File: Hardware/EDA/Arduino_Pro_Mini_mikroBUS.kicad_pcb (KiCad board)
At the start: 4 copper layers, 38.1 x 69.8 mm, 36 parts, among them CON1 BARREL_JACK, J1 HEADER_F_2.54MM_1R8P_ST_AU_PTH, J2 HEADER_F_2.54MM_1R8P_ST_AU_PTH, J3 HEADER_F_2.54MM_1R12P_ST_AU_P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, J4 HEADER_F_2.54MM_1R12P_ST_AU_P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, J5 Molex_0475710001, J6 HEADER_F_2.54MM_1R2P_ST_AU_PTH, M1 FID, M2 FID, M3 FID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

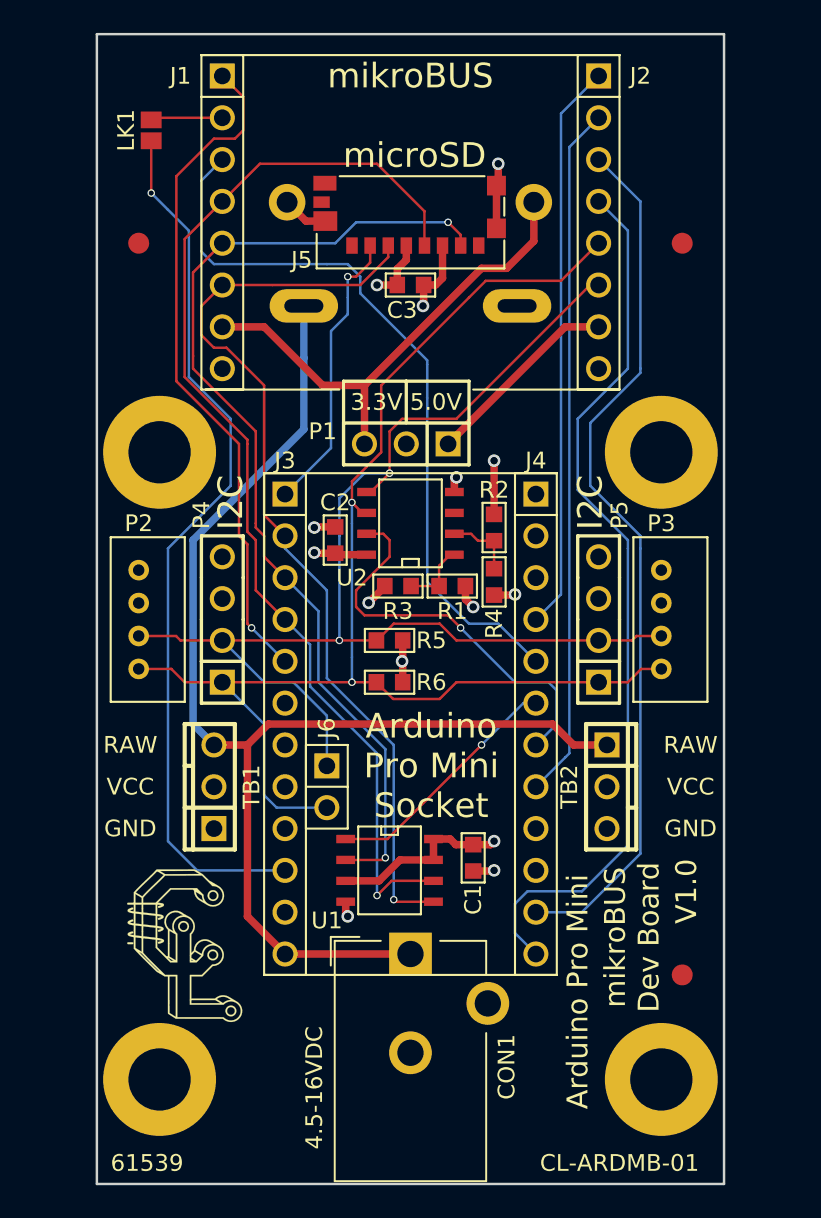
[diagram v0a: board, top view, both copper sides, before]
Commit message: Removed barrel jack connector due to interference with Arduino Pro Mini. Updated schematic, layout and generated new gerbers. Added BOM file.
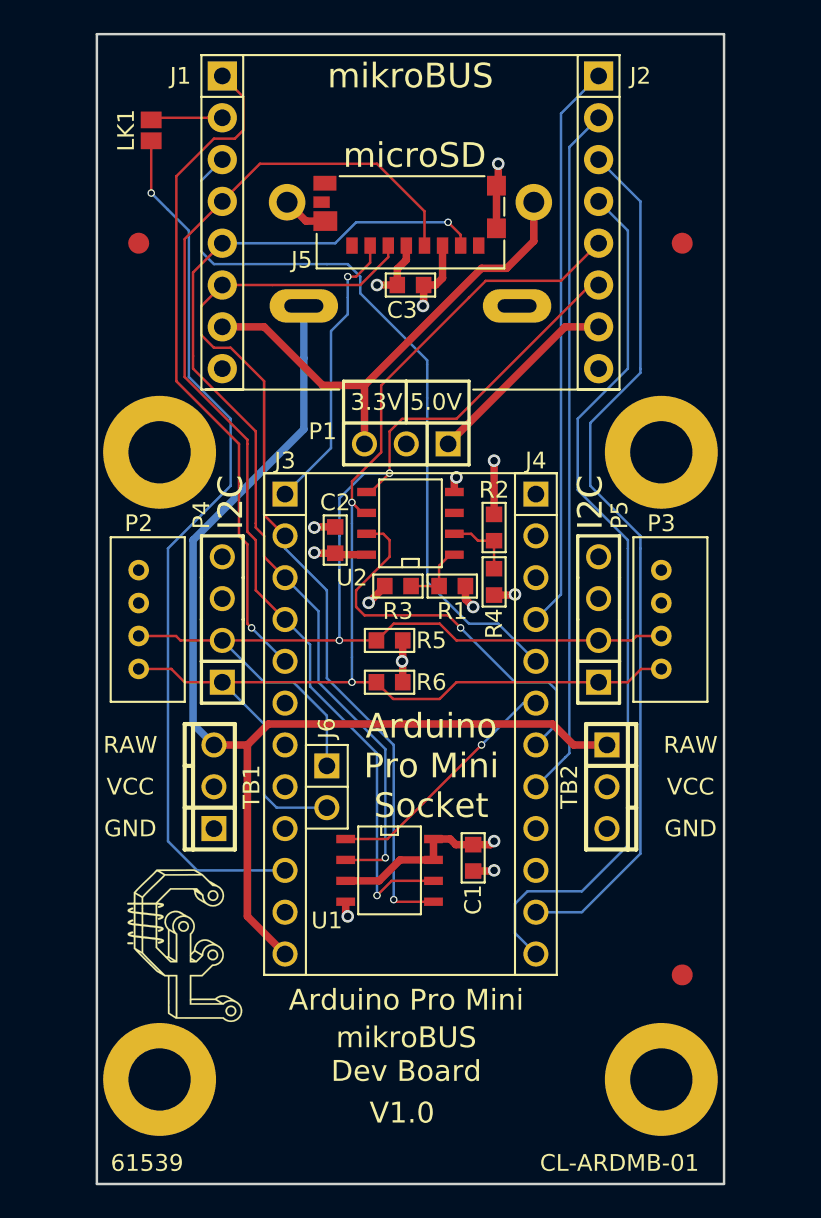
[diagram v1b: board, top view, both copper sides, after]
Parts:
- removed CON1: BARREL_JACK, Connect:Barrel_Jack_CUI_PJ-102AH
- TB2: footprint Terminal_Block:TB_100MIL_1R3P_PTH -> TB_100MIL_1R3P_PTH
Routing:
- net RAW: track 76.2 -> 68.6 mm
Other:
- board text removed: "4.5-16VDC"

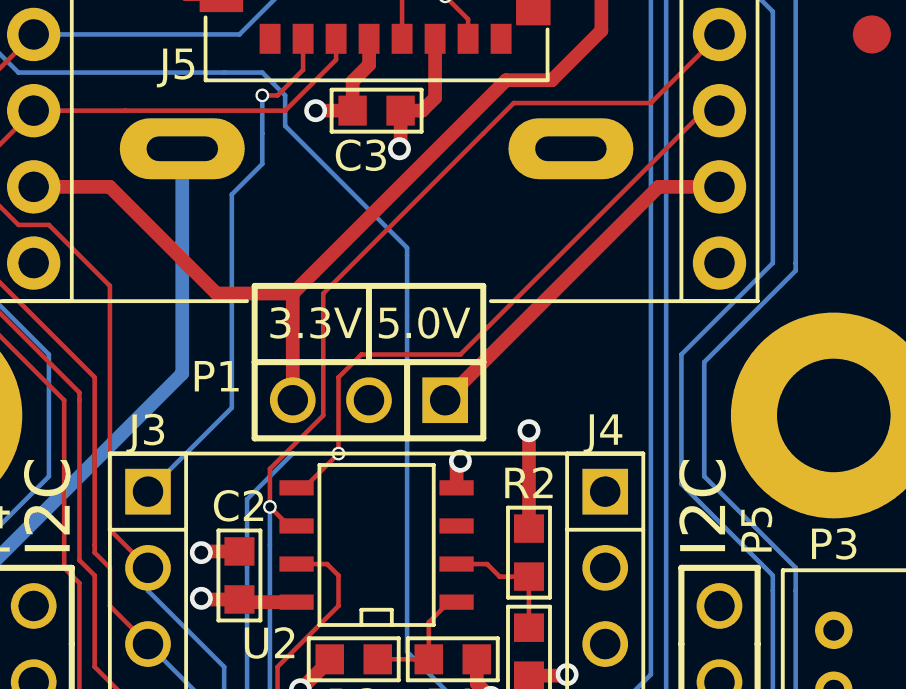
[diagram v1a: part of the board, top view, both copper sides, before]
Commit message: Move location of P1 down slightly to allow more room for mikroBUS module PCB.
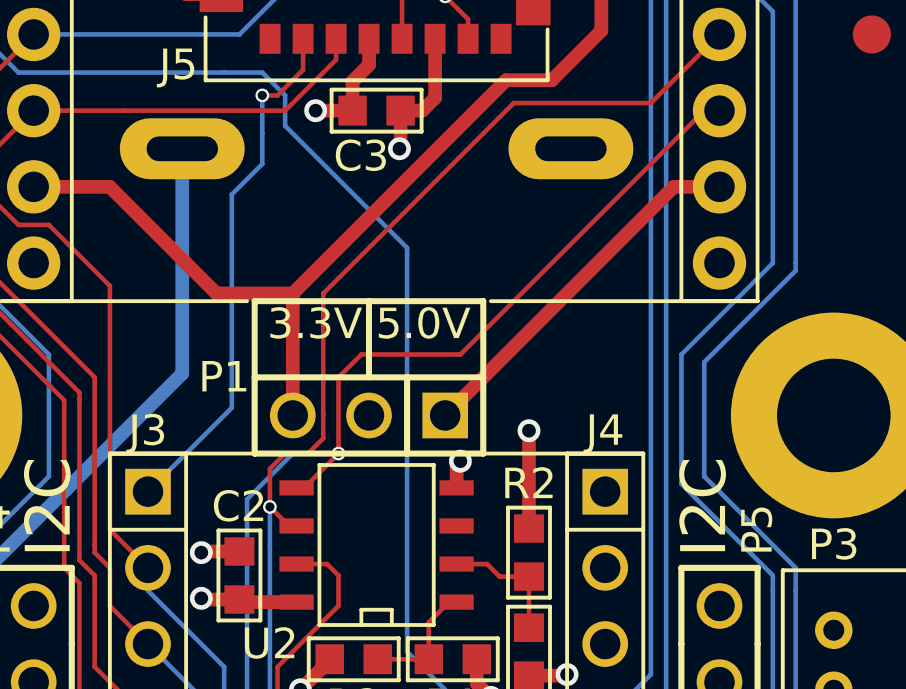
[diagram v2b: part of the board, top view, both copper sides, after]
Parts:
- moved P1 0.51 mm to (79.8, 57.1)
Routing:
- net 3.3V: track 29.9 -> 30.5 mm
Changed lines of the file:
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@@
     (thickness 1.6)
     (drawings 36)
-    (tracks 318)
+    (tracks 320)
     (zones 0)
     (modules 35)
@@
     (pad 2 thru_hole circle (at 27.8892 -7.493 90) (size 2.2225 2.2225) (drill 1.27) (layers *.Cu *.Mask)
       (net 2 GND))
-    (model C:/Engineering/KiCAD_Libraries/3D/Battery_Holders/VRML/KEYSTONE_2462.wrl
+    (model C:/Engineering/KiCAD_Libraries/3D/Battery_Holders/VRML/KEYSTONE_2462.wrl_
       (at (xyz 0.03 0 0))
       (scale (xyz 1 1 1))
@@
   )
   (module Header:HEADER_M_2.54MM_1R3P_ST_AU_PTH locked (layer F.Cu)
-    (at 79.756 56.642 180)
+    (at 79.756 57.15 180)
     (tags Header)
-    (fp_text reference P1 (at 5.08 0.762 180) (layer F.SilkS)
+    (fp_text reference P1 (at 4.826 1.27 180) (layer F.SilkS)
       (effects (font (size 1.016 1.016) (thickness 0.127)))
     )
@@
     (pad 1 thru_hole rect (at -2.54 0 180) (size 1.524 1.524) (drill 1.016) (layers *.Cu *.Mask)
       (net 11 5.0V))
-    (model C:\Engineering\KiCAD_Libraries\3D\Headers\HEADER_M_2.54MM_1R3P_ST_AU_PTH.wrl
+    (model C:/Engineering/KiCAD_Libraries/3D/Headers/VRML/HEADER_M_2.54MM_1R3P_ST_AU_PTH.wrl
       (at (xyz 0 0 0))
       (scale (xyz 1 1 1))
@@
     (pad 1 thru_hole rect (at -1.27 0 270) (size 1.524 1.524) (drill 1.016) (layers *.Cu *.Mask)
       (net 10 SDA))
-    (model C:/Engineering/KiCAD_Libraries/3D/Headers/VRML/HEADER_F_2.54MM_1R2P_ST_SN_PTH.wrl
+    (model C:/Engineering/KiCAD_Libraries/3D/Headers/VRML/HEADER_F_2.54MM_1R2P_ST_AU_PTH.wrl
       (at (xyz 0 0 0))
       (scale (xyz 1 1 1))
@@
   (gr_line (start 83.82 53.34) (end 92.71 53.34) (angle 90) (layer F.SilkS) (width 0.127))
   (gr_line (start 67.564 53.34) (end 75.692 53.34) (angle 90) (layer F.SilkS) (width 0.127))
-  (gr_line (start 75.946 52.832) (end 75.946 55.372) (angle 90) (layer F.SilkS) (width 0.2))
-  (gr_line (start 83.566 52.832) (end 83.566 55.372) (angle 90) (layer F.SilkS) (width 0.2))
-  (gr_line (start 79.756 52.832) (end 75.946 52.832) (angle 90) (layer F.SilkS) (width 0.2))
-  (gr_line (start 79.756 52.832) (end 83.566 52.832) (angle 90) (layer F.SilkS) (width 0.2))
-  (gr_line (start 79.756 55.372) (end 79.756 52.832) (angle 90) (layer F.SilkS) (width 0.2))
+  (gr_line (start 75.946 53.34) (end 75.946 55.88) (angle 90) (layer F.SilkS) (width 0.2))
+  (gr_line (start 83.566 53.34) (end 83.566 55.88) (angle 90) (layer F.SilkS) (width 0.2))
+  (gr_line (start 79.756 53.34) (end 75.946 53.34) (angle 90) (layer F.SilkS) (width 0.2))
+  (gr_line (start 79.756 53.34) (end 83.566 53.34) (angle 90) (layer F.SilkS) (width 0.2))
+  (gr_line (start 79.756 55.88) (end 79.756 53.34) (angle 90) (layer F.SilkS) (width 0.2))
   (gr_text RAW (at 97.028 74.93) (layer F.SilkS)
     (effects (font (size 1.016 1.016) (thickness 0.2032)))
@@
   (segment (start 78.66 45.292) (end 78.66 44.595) (width 0.1524) (layer F.Cu) (net 3))
   (segment (start 76.962 46.99) (end 78.66 45.292) (width 0.1524) (layer F.Cu) (net 3))
+  (segment (start 77.216 57.15) (end 77.216 53.086) (width 0.4572) (layer F.Cu) (net 4) (status 400000))
   (segment (start 68.58 49.53) (end 71.12 49.53) (width 0.4572) (layer F.Cu) (net 4))
   (segment (start 74.676 53.086) (end 77.216 53.086) (width 0.4572) (layer F.Cu) (net 4))
   (segment (start 71.12 49.53) (end 74.676 53.086) (width 0.4572) (layer F.Cu) (net 4))
-  (segment (start 77.216 56.642) (end 77.216 53.086) (width 0.4572) (layer F.Cu) (net 4))
   (segment (start 87.503 44.323) (end 85.852 45.974) (width 0.4572) (layer F.Cu) (net 4))
   (segment (start 87.503 44.323) (end 87.503 41.9608) (width 0.4572) (layer F.Cu) (net 4))
@@
   (segment (start 66.04 68.58) (end 68.58 68.58) (width 0.1524) (layer F.Cu) (net 10))
   (segment (start 65.77 68.31) (end 66.04 68.58) (width 0.1524) (layer F.Cu) (net 10))
-  (segment (start 82.296 56.642) (end 89.408 49.53) (width 0.4572) (layer F.Cu) (net 11))
-  (segment (start 89.408 49.53) (end 91.44 49.53) (width 0.4572) (layer F.Cu) (net 11))
+  (segment (start 82.296 57.15) (end 89.916 49.53) (width 0.4572) (layer F.Cu) (net 11) (status 400000))
+  (segment (start 89.916 49.53) (end 91.44 49.53) (width 0.4572) (layer F.Cu) (net 11) (status 800000))
+  (segment (start 78.232 57.15) (end 78.232 57.912) (width 0.1524) (layer F.Cu) (net 12))
+  (segment (start 83.566 47.752) (end 78.232 53.086) (width 0.1524) (layer F.Cu) (net 12))
+  (segment (start 76.454 58.928) (end 76.454 60.198) (width 0.1524) (layer F.Cu) (net 12))
+  (segment (start 78.232 57.15) (end 78.232 53.086) (width 0.1524) (layer F.Cu) (net 12))
+  (segment (start 76.962 58.42) (end 76.454 58.928) (width 0.1524) (layer F.Cu) (net 12))
+  (segment (start 77.724 58.42) (end 76.962 58.42) (width 0.1524) (layer F.Cu) (net 12))
+  (segment (start 78.232 57.912) (end 77.724 58.42) (width 0.1524) (layer F.Cu) (net 12))
   (segment (start 68.58 71.12) (end 71.12 73.66) (width 0.1524) (layer B.Cu) (net 12))
   (segment (start 71.882 78.74) (end 74.93 78.74) (width 0.1524) (layer B.Cu) (net 12))
@@
   (segment (start 71.12 73.66) (end 71.12 77.978) (width 0.1524) (layer B.Cu) (net 12))
   (segment (start 76.454 71.12) (end 76.454 69.596) (width 0.1524) (layer B.Cu) (net 12))
+  (via (at 76.454 71.12) (size 0.4572) (drill 0.3048) (layers F.Cu B.Cu) (net 12))
+  (segment (start 76.454 61.468) (end 76.454 60.198) (width 0.1524) (layer B.Cu) (net 12))
+  (segment (start 76.454 69.596) (end 76.454 61.468) (width 0.1524) (layer B.Cu) (net 12))
   (via (at 76.454 60.198) (size 0.4572) (drill 0.3048) (layers F.Cu B.Cu) (net 12))
-  (segment (start 76.454 69.596) (end 76.454 61.468) (width 0.1524) (layer B.Cu) (net 12))
-  (segment (start 76.454 61.468) (end 76.454 60.198) (width 0.1524) (layer B.Cu) (net 12))
-  (via (at 76.454 71.12) (size 0.4572) (drill 0.3048) (layers F.Cu B.Cu) (net 12))
   (segment (start 91.44 44.45) (end 89.154 46.736) (width 0.1524) (layer F.Cu) (net 12))
   (segment (start 84.582 46.736) (end 83.566 47.752) (width 0.1524) (layer F.Cu) (net 12))
@@
   (segment (start 93.218 71.12) (end 91.44 71.12) (width 0.1524) (layer F.Cu) (net 12))
   (segment (start 94.028 70.31) (end 93.218 71.12) (width 0.1524) (layer F.Cu) (net 12))
-  (segment (start 77.47 57.912) (end 78.232 57.15) (width 0.1524) (layer F.Cu) (net 12))
-  (segment (start 78.232 57.15) (end 78.232 53.086) (width 0.1524) (layer F.Cu) (net 12))
-  (segment (start 76.454 58.928) (end 77.47 57.912) (width 0.1524) (layer F.Cu) (net 12))
-  (segment (start 76.454 60.198) (end 76.454 58.928) (width 0.1524) (layer F.Cu) (net 12))
-  (segment (start 83.566 47.752) (end 78.232 53.086) (width 0.1524) (layer F.Cu) (net 12))
   (segment (start 76.454 60.198) (end 77.089 60.833) (width 0.1524) (layer F.Cu) (net 12))
   (segment (start 83.566 47.752) (end 83.566 47.752) (width 0.1524) (layer F.Cu) (net 12))

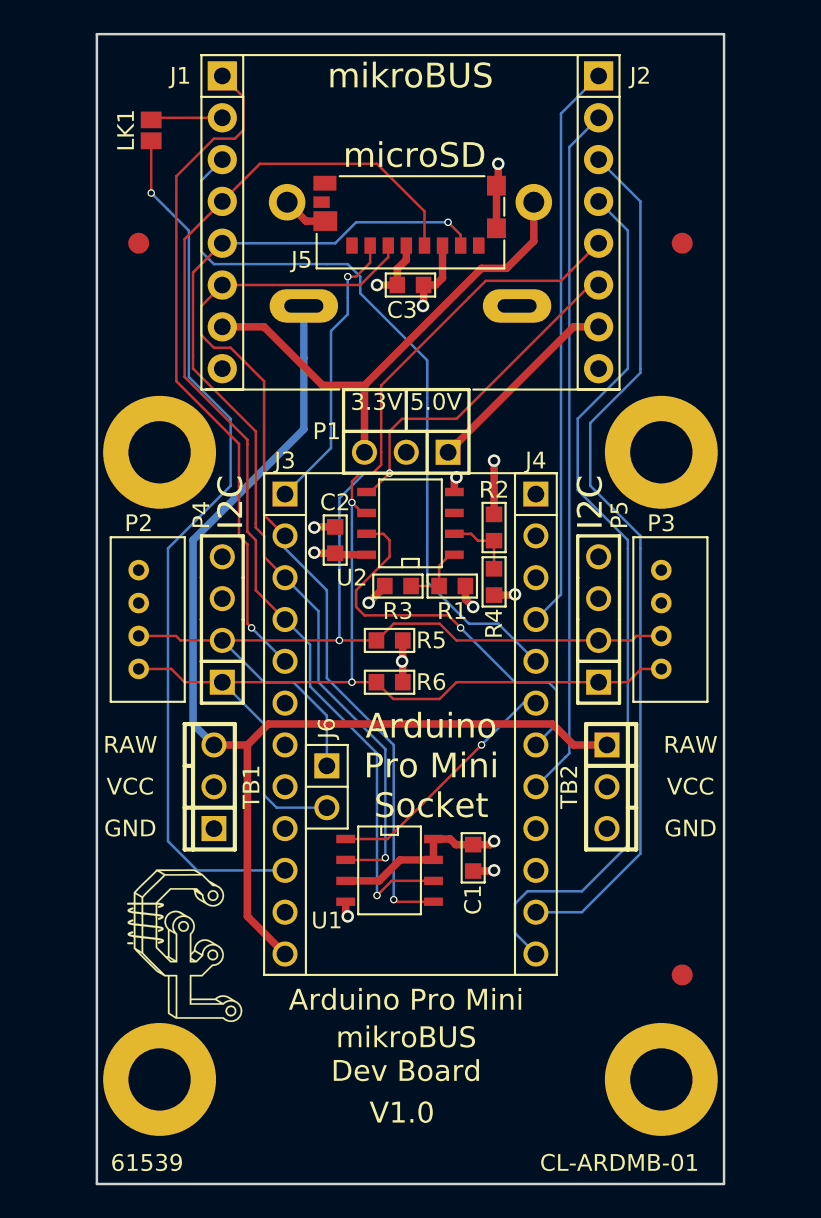
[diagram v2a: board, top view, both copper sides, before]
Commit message: Changed PCB outline/size to accomodate mounting holes, but still fit in enclosure. Regenerated Gerbers and PCB render images.
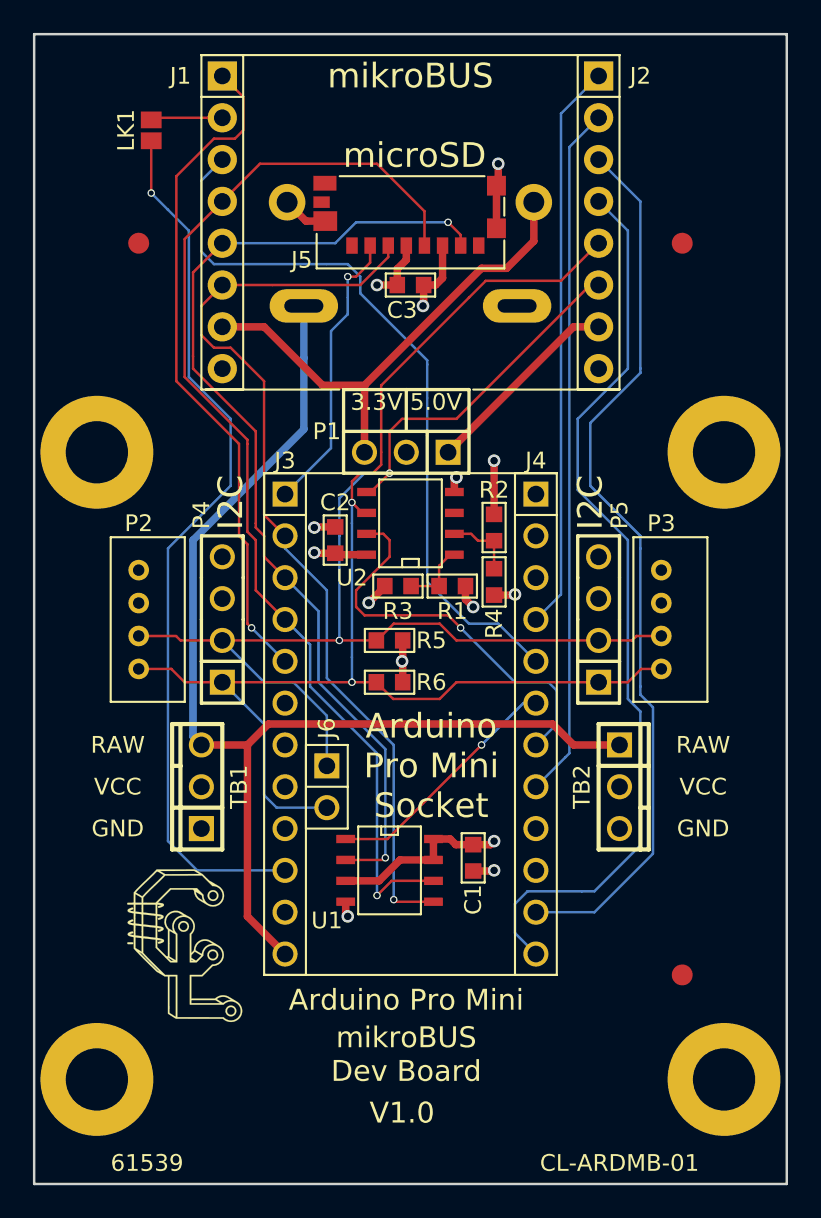
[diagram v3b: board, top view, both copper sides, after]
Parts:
- moved MH2 3.81 mm to (99.1, 57.1)
- moved MH4 3.81 mm to (99.1, 95.2)
- moved MH1 3.81 mm to (61.0, 57.1)
- moved MH3 3.81 mm to (61.0, 95.2)
- moved TB1 0.76 mm to (67.3, 77.5)
- moved TB2 0.76 mm to (92.7, 77.5)
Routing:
- net RAW: track 68.6 -> 69.8 mm
- net TXD: track 54.3 -> 55.4 mm
- net RXD: track 53.6 -> 54.6 mm
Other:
- board size 38.1 x 69.8 mm -> 45.7 x 69.8 mm

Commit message: Initial updates based on first build and testing.  Final updates to be pushed in subsequent commit(s).
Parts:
- moved G1 1.61 mm to (64.8, 87.6)
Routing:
- net 3.3V: track 30.5 -> 21.0 mm
- net 5.0V: track 12.3 -> 19.7 mm
- net RAW: track 69.8 -> 74.1 mm
- net SDA: track 77.2 -> 80.6 mm
- net GND: track 18.5 -> 17.6 mm, vias 8 -> 9
- net SCL: track 82.5 -> 83.3 mm
- net MOSI: track 57.2 -> 57.6 mm, vias 1 -> 2
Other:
- board text added: "3.3V"
- board text added: "5.0V"
- board text added: "???"
- board text added: "Corrections made: Corrected pin numbering of 2xAA battery holder footprint to match schematic decal Corrected pin numbering of 1x9V battery holder footprint to match schematic decal Re-layed out 2xAA battery traces Re-layed out 1x9V battery traces Added silkscreen pin names to Grove connector Add silkscreen orientation to Arduino socket"
- board text added: "Corrections needed: RTC needs crystal and caps Add silkscreen pin names to mikroBUS connector Check FL127 footprint against Winbond footprint"
- board text added: "MISO"
- board text added: "MOSI"
- board text added: "RST"
- board text added: "RXD"
- board text added: "SCK"
- board text added: "SCL"
- board text added: "SDA"
- board text added: "TXD"
- board text added: "V1.1"
- board text removed: "V1.0"

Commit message: Few more updates.
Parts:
- removed R1, R2, R3, R4: 4.7k, Passive:R0603
- added C4: 12pF, Passive:0603, F.Cu at (83.9, 65.7)
- added C5: 12pF, Passive:0603, F.Cu at (84.8, 59.1)
- added Y1: 32.768k, Crystals:Crystal_SMD_G8-2pin_3.2x1.5mm, F.Cu at (84.8, 62.7)
- moved M1 2.54 mm to (99.1, 88.9)
- moved M2 2.54 mm to (99.1, 44.5)
- moved M3 2.54 mm to (61.0, 44.5)
- moved LK1 1.52 mm to (62.7, 37.6)
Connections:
- J3 pad 6: (no net) -> A1
- J3 pad 7: (no net) -> A2
- J3 pad 8: (no net) -> A3
- J4 pad 1: (no net) -> D9
- J4 pad 2: (no net) -> D8
- J4 pad 3: (no net) -> D7
- J5 pad 1: (no net) -> Net-(J5-Pad1)
- J5 pad 12: (no net) -> Net-(J5-Pad12)
- J5 pad 13: (no net) -> Net-(J5-Pad13)
- J5 pad 8: (no net) -> Net-(J5-Pad8)
- M1 pad ~: (no net) -> Net-(M1-Pad~)
- M2 pad ~: (no net) -> Net-(M2-Pad~)
- M3 pad ~: (no net) -> Net-(M3-Pad~)
- U2 pad 3: (no net) -> Net-(U2-Pad3)
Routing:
- net VCC: track 25.7 -> 21.0 mm, vias 6 -> 4
- net D3: track 24.6 -> 19.9 mm
- net mikroBUS_RST: track 4.37 -> 5.89 mm
- net RST: track 54.0 -> 54.6 mm
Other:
- board text added: "AN"
- board text added: "CS"
- board text added: "Corrections made: Corrected pin numbering of 2xAA battery holder footprint to match schematic decal Corrected pin numbering of 1x9V battery holder footprint to match schematic decal Re-layed out 2xAA battery traces Re-layed out 1x9V battery traces Added silkscreen pin names to Grove connector Add silkscreen orientation to Arduino socket Add silkscreen pin names to mikroBUS connector"
- board text added: "Corrections needed: RTC needs crystal and caps Check FL127 footprint against Winbond footprint Add level shifter for microSD socket?"
- board text added: "INT"
- board text added: "PWM"
- board text removed: "???"
- board text removed: "Corrections made: Corrected pin numbering of 2xAA battery holder footprint to match schematic decal Corrected pin numbering of 1x9V battery holder footprint to match schematic decal Re-layed out 2xAA battery traces Re-layed out 1x9V battery traces Added silkscreen pin names to Grove connector Add silkscreen orientation to Arduino socket"
- board text removed: "Corrections needed: RTC needs crystal and caps Add silkscreen pin names to mikroBUS connector Check FL127 footprint against Winbond footprint"
